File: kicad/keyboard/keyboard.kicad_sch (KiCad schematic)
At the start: 119 parts, among them SW1 MX_SWITCH, SW10 MX_SWITCH, SW11 MX_SWITCH, SW12 MX_SWITCH, SW13 MX_SWITCH, SW14 MX_SWITCH, SW15 MX_SWITCH, SW16 MX_SWITCH, SW17 MX_SWITCH, SW18 MX_SWITCH, SW19 MX_SWITCH, SW2 MX_SWITCH, SW20 MX_SWITCH, SW21 MX_SWITCH, SW22 MX_SWITCH, SW23 MX_SWITCH, SW24 MX_SWITCH, SW25 MX_SWITCH, SW26 MX_SWITCH, SW27 MX_SWITCH, SW28 MX_SWITCH, SW29 MX_SWITCH, SW3 MX_SWITCH, SW30 MX_SWITCH, SW31 MX_SWITCH, SW32 MX_SWITCH, SW33 MX_SWITCH, SW34 MX_SWITCH, SW35 MX_SWITCH, SW36 MX_SWITCH, SW37 MX_SWITCH, SW38 MX_SWITCH, SW39 MX_SWITCH, SW4 MX_SWITCH, SW40 MX_SWITCH, SW41 MX_SWITCH, SW42 MX_SWITCH, SW43 MX_SWITCH, SW44 MX_SWITCH, SW45 MX_SWITCH, SW46 MX_SWITCH, SW47 MX_SWITCH, SW48 MX_SWITCH, SW49 MX_SWITCH, SW5 MX_SWITCH, SW50 MX_SWITCH, SW51 MX_SWITCH, SW52 MX_SWITCH, SW53 MX_SWITCH, SW54 MX_SWITCH, SW55 MX_SWITCH, SW56 MX_SWITCH, SW57 MX_SWITCH, SW58 MX_SWITCH, SW59 MX_SWITCH, SW6 MX_SWITCH, SW7 MX_SWITCH, SW8 MX_SWITCH, SW9 MX_SWITCH

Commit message: Increase the number of keys
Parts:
- added D60: D, symbol Device:D
- added SW60: MX_SWITCH, symbol Switch:SW_Push_45deg
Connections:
- net COL0: now also SW13.1, SW25.1, SW37.1, SW49.1; no longer SW12.1, SW23.1, SW34.1, SW45.1
- net COL1: now also SW14.1, SW26.1, SW38.1, SW50.1; no longer SW13.1, SW24.1, SW35.1, SW46.1
- net COL10: now also SW23.1, SW35.1, SW47.1, SW59.1; no longer SW22.1, SW33.1, SW44.1, SW55.1
- net COL11: now also SW12.1, SW24.1, SW36.1, SW48.1, SW60.1; no longer SW56.1, SW57.1
- net COL2: now also SW15.1, SW27.1, SW39.1, SW51.1; no longer SW14.1, SW25.1, SW36.1, SW47.1
- net COL3: now also SW16.1, SW28.1, SW40.1, SW52.1; no longer SW15.1, SW26.1, SW37.1, SW48.1
- net COL4: now also SW17.1, SW29.1, SW41.1, SW53.1; no longer SW16.1, SW27.1, SW38.1, SW49.1
- net COL5: now also SW18.1, SW30.1, SW42.1, SW54.1; no longer SW17.1, SW28.1, SW39.1, SW50.1
- net COL6: now also SW19.1, SW31.1, SW43.1, SW55.1; no longer SW18.1, SW29.1, SW40.1, SW51.1
- net COL7: now also SW20.1, SW32.1, SW44.1, SW56.1; no longer SW19.1, SW30.1, SW41.1, SW52.1
- net COL8: now also SW21.1, SW33.1, SW45.1, SW57.1; no longer SW20.1, SW31.1, SW42.1, SW53.1
- net COL9: now also SW22.1, SW34.1, SW46.1, SW58.1; no longer SW21.1, SW32.1, SW43.1, SW54.1
- net ROW0: now also D56.1 (K), D58.1 (K), D60.1 (K); no longer D45.1 (K), D46.1 (K), D47.1 (K), D48.1 (K)
- net ROW1: now also D45.1 (K), D46.1 (K), D47.1 (K), D48.1 (K); no longer D34.1 (K), D35.1 (K), D36.1 (K), D56.1 (K), D58.1 (K)
- net ROW2: now also D34.1 (K), D35.1 (K), D36.1 (K); no longer D23.1 (K), D24.1 (K)
- net ROW3: now also D23.1 (K), D24.1 (K); no longer D12.1 (K)
- net ROW4: now also D12.1 (K)
- removed net COL12: A1.22 (GPIO17), SW58.1, SW59.1
- new net: D60.2 (A), SW60.2
- no-connect marks 16 -> 17

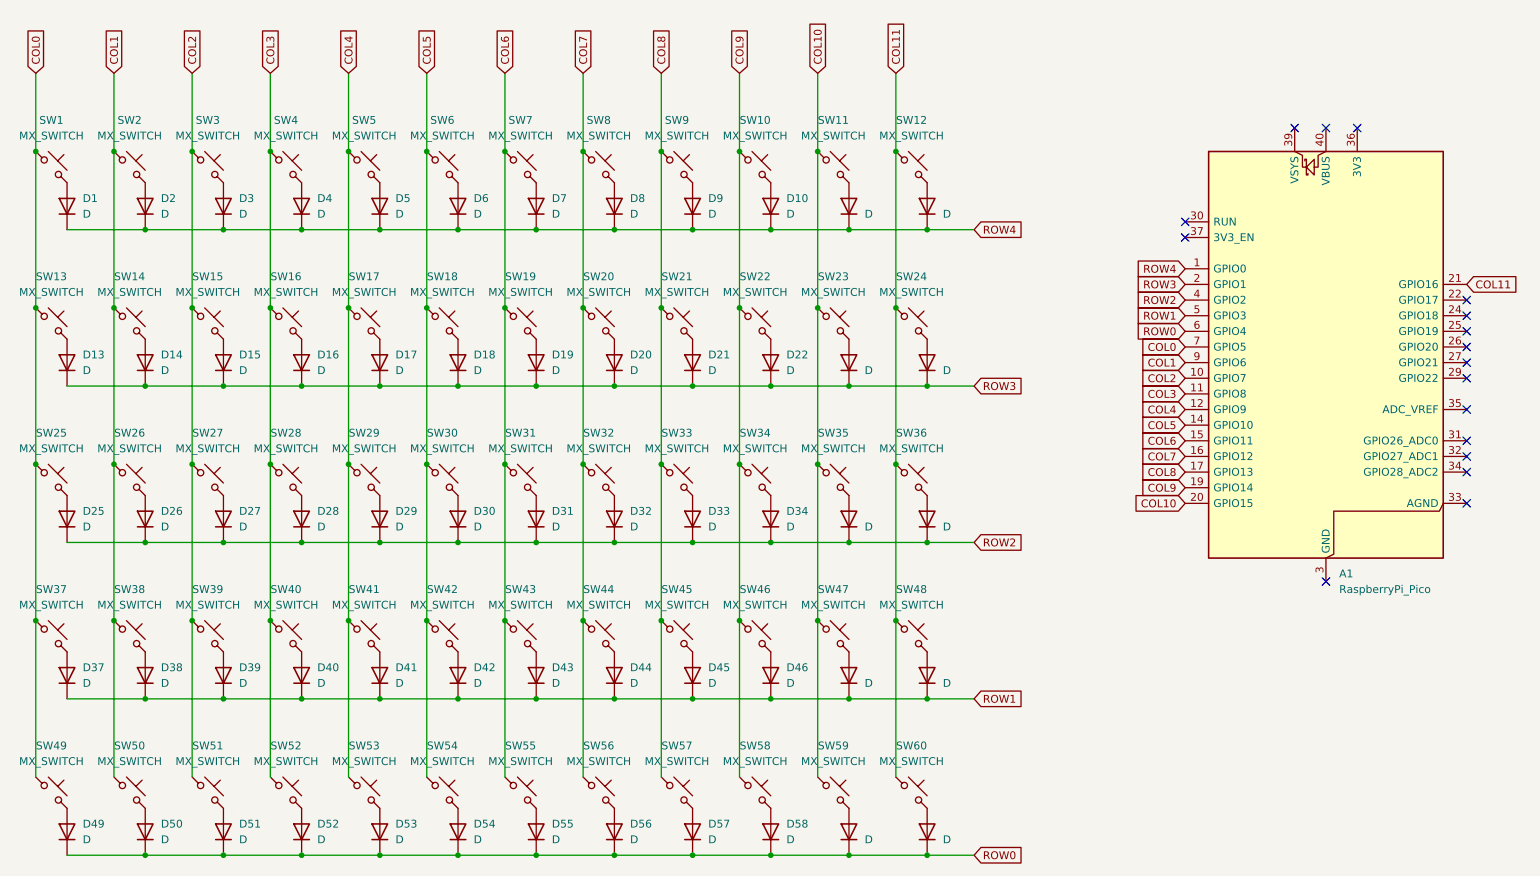
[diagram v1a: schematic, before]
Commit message: Assign footprints
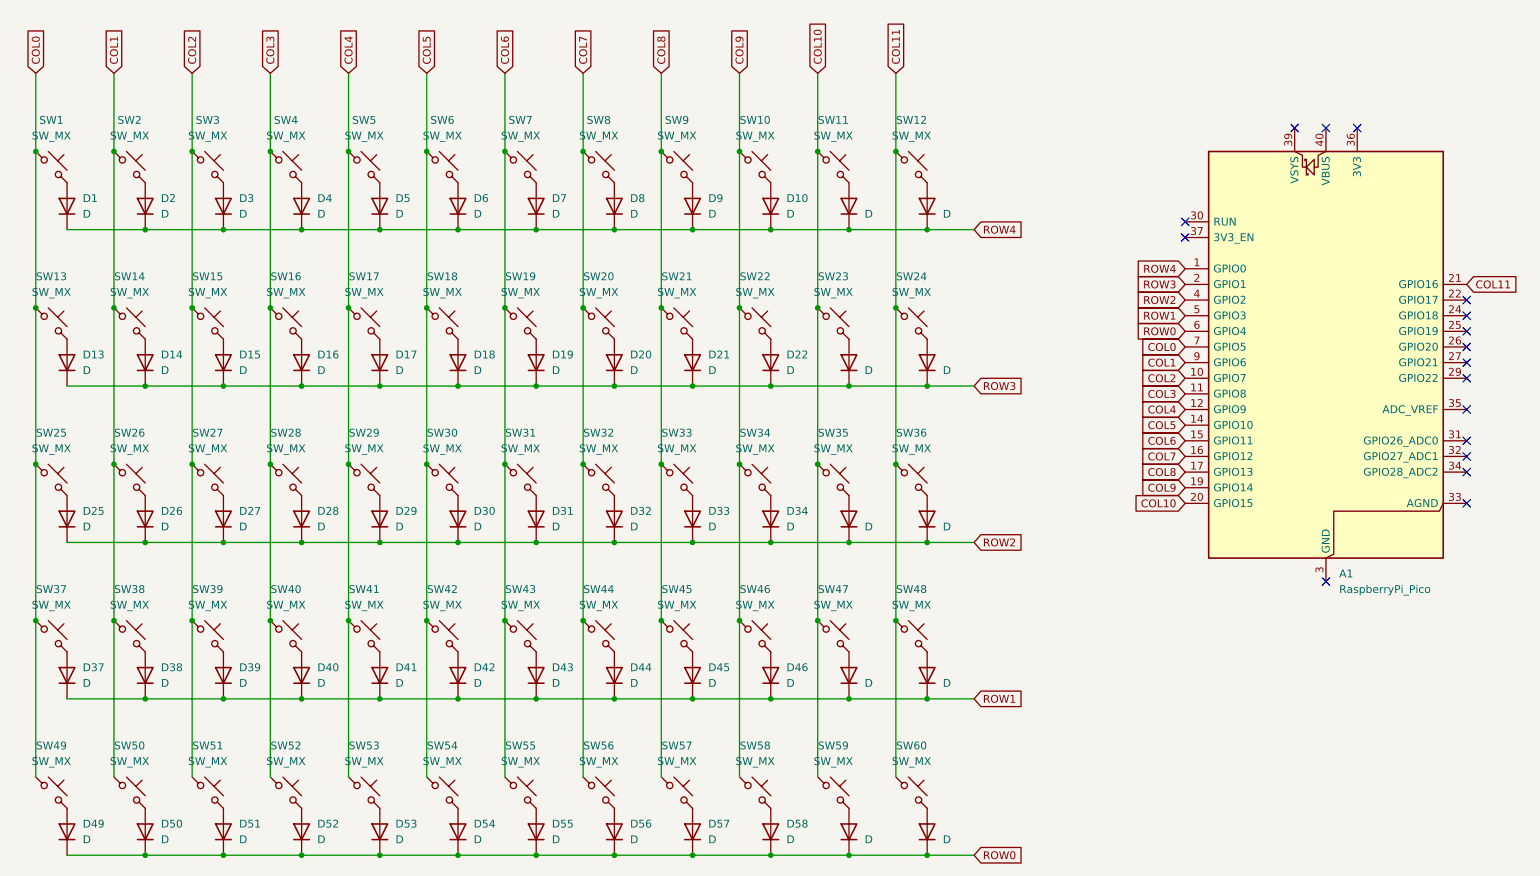
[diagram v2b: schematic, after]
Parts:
- D1, D10, D11, D12, D13, D14, D15, D16, D17, D18, D19, D2, D20, D21, D22, D23, D24, D25, D26, D27, D28, D29, D3, D30, D31, D32, D33, D34, D35, D36, D37, D38, D39, D4, D40, D41, D42, D43, D44, D45, D46, D47, D48, D49, D5, D50, D51, D52, D53, D54, D55, D56, D57, D58, D59, D6, D60, D7, D8, D9: footprint (none) -> Diode_THT:D_DO-35_SOD27_P2.54mm_Vertical_AnodeUp
- SW1, SW10, SW11, SW12, SW13, SW14, SW15, SW16, SW17, SW18, SW19, SW2, SW20, SW21, SW22, SW23, SW24, SW25, SW26, SW27, SW28, SW29, SW3, SW30, SW31, SW32, SW33, SW34, SW35, SW36, SW37, SW38, SW39, SW4, SW40, SW41, SW42, SW43, SW44, SW45, SW46, SW47, SW48, SW49, SW5, SW50, SW51, SW52, SW53, SW54, SW55, SW56, SW57, SW58, SW59, SW6, SW60, SW7, SW8, SW9: value MX_SWITCH -> SW_MX; footprint (none) -> Button_Switch_Keyboard:SW_Cherry_MX_1.00u_PCB
